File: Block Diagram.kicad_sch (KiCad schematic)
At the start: 0 parts

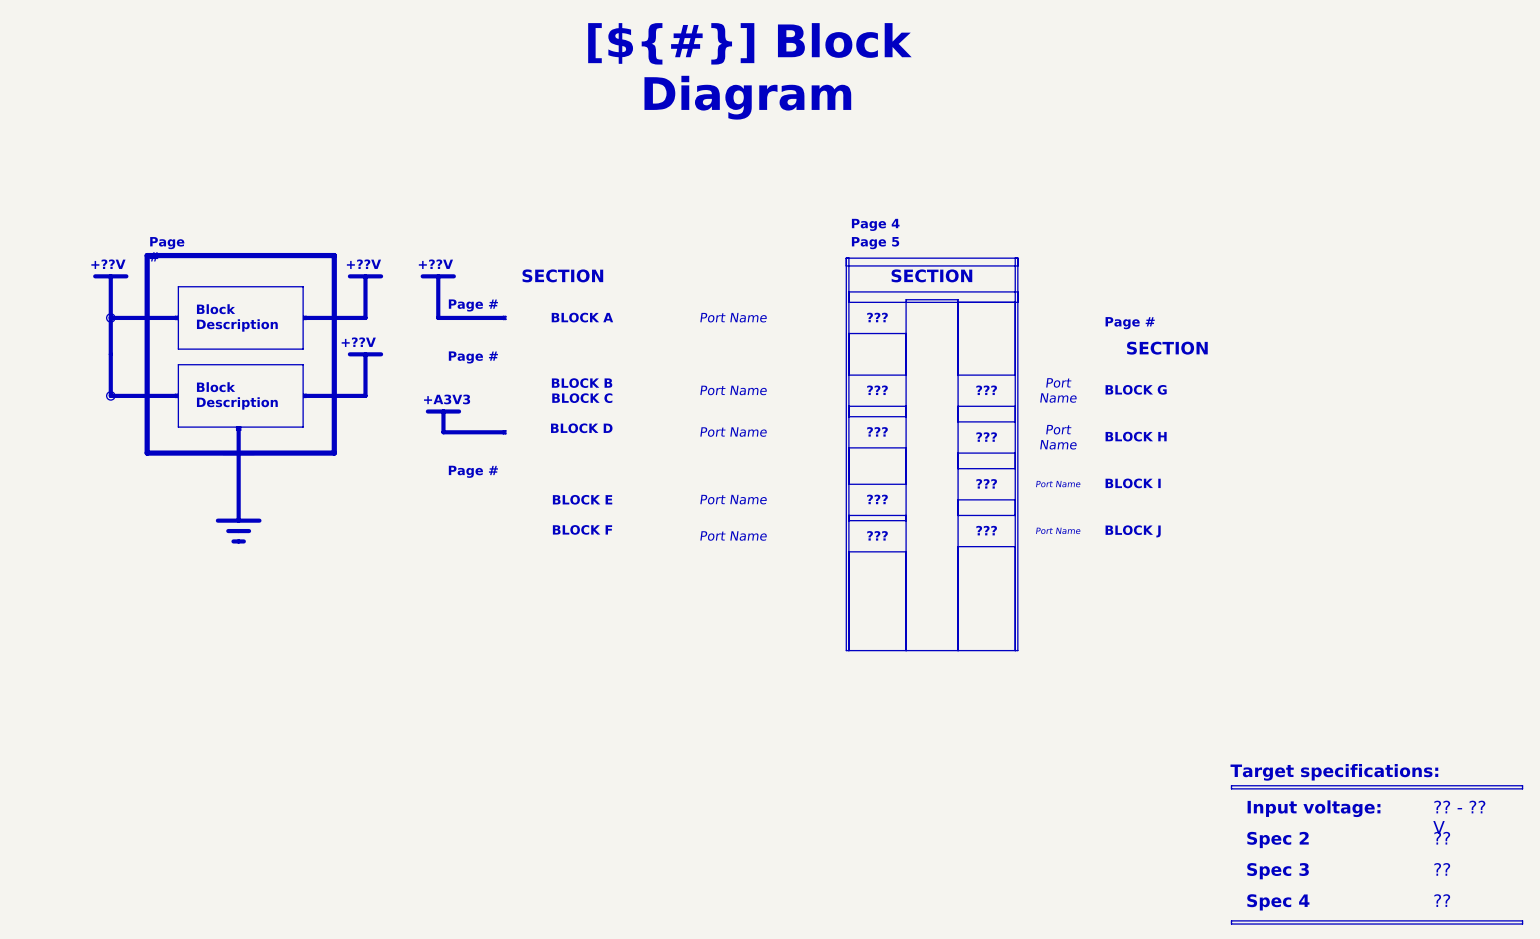
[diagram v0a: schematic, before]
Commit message: Fill template pages: block diagram, power sequencing, cover notes, architecture
- Block Diagram redrawn from the real design: phase path (MR60PW, shunts),
  current and voltage channels with their gains and bandwidths, AD7606C-18,
  power chain, target specifications
- Power - Sequencing: start-up curves taken from the LTspice simulations
  (boost soft-start, analog rails) and rail table with sources, levels
  and timings
- Cover page: real design notes instead of the template examples
- Project Architecture: power-supply block documented, contiguous page
  numbers (Power Supply is page 6)
- Revision History: one column fed by the [Unreleased] changelog section
- sheet titles shortened so they fit the cover-page index: INA241 - Phase
  Sensing, Power Supply - Analog Rails

Sheet-level polylines carry no fill attribute (KiBot schematic reader).

Co-Authored-By: Claude Opus 5.5 <noreply@anthropic.com>
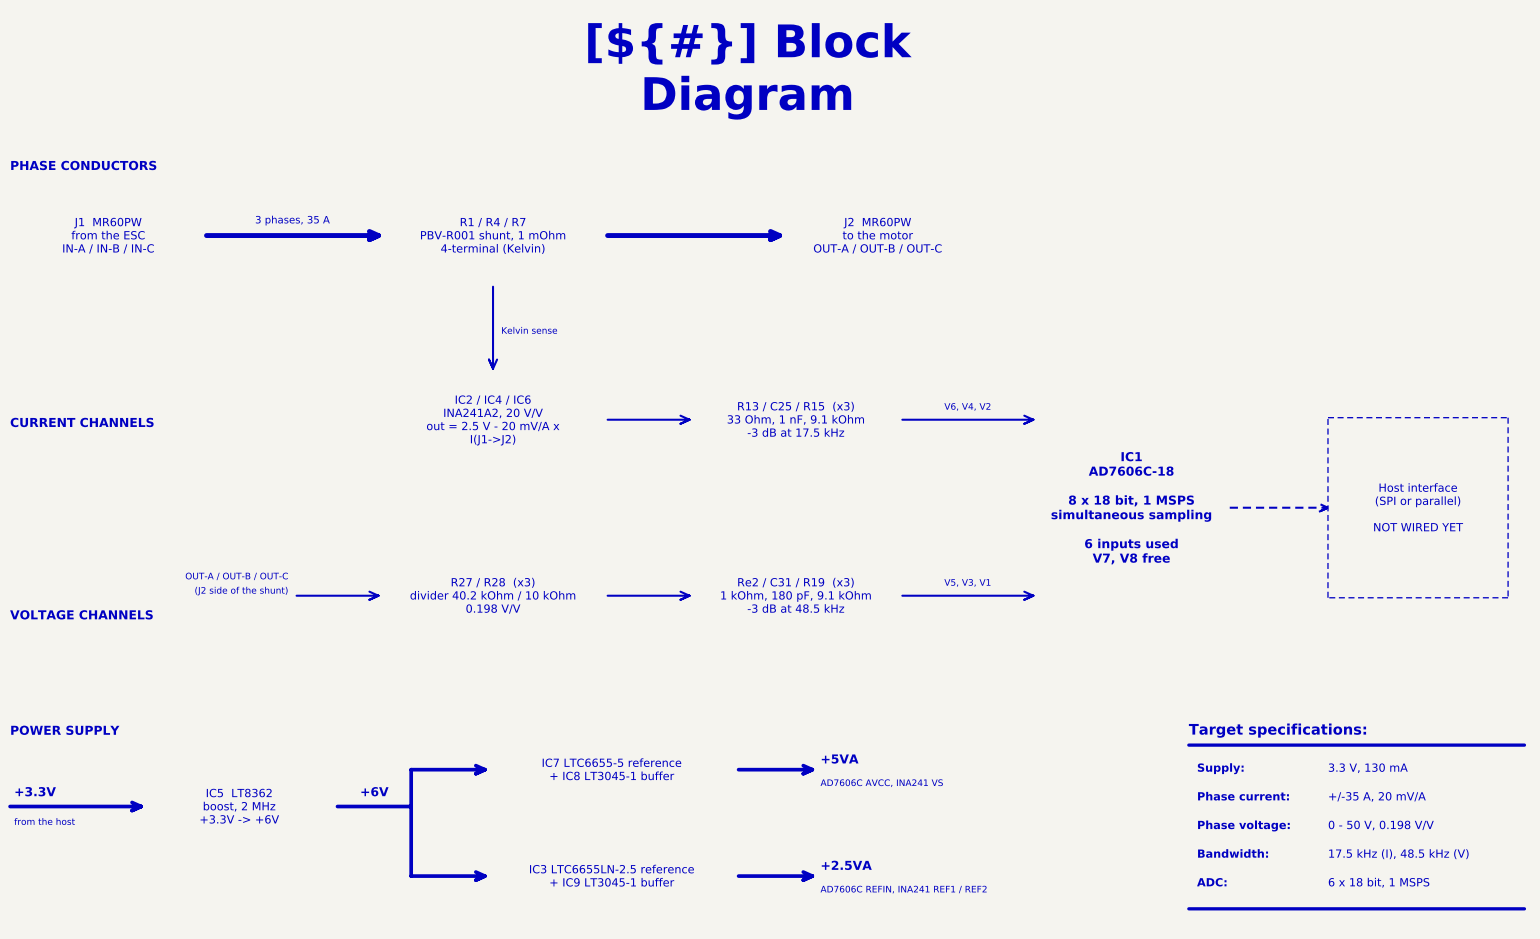
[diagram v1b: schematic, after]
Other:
- note added: "(J2 side of the shunt)"
- note added: "+/-35 A, 20 mV/A"
- note added: "+2.5VA"
- note added: "+3.3V"
- note added: "+5VA"
- note added: "+6V"
- note added: "0 - 50 V, 0.198 V/V"
- note added: "17.5 kHz (I), 48.5 kHz (V)"
- note added: "3 phases, 35 A"
- note added: "3.3 V, 130 mA"
- note added: "6 x 18 bit, 1 MSPS"
- note added: "AD7606C AVCC, INA241 VS"
- note added: "AD7606C REFIN, INA241 REF1 / REF2"
- note added: "ADC:"
- note added: "Bandwidth:"
- note added: "CURRENT CHANNELS"
- note added: "Kelvin sense"
- note added: "OUT-A / OUT-B / OUT-C"
- note added: "PHASE CONDUCTORS"
- note added: "POWER SUPPLY"
- note added: "Phase current:"
- note added: "Phase voltage:"
- note added: "Supply:"
- note added: "Target specifications:"
- note added: "V5, V3, V1"
- note added: "V6, V4, V2"
- note added: "VOLTAGE CHANNELS"
- note added: "from the host"
- note removed: "+??V"
- note removed: "+A3V3"

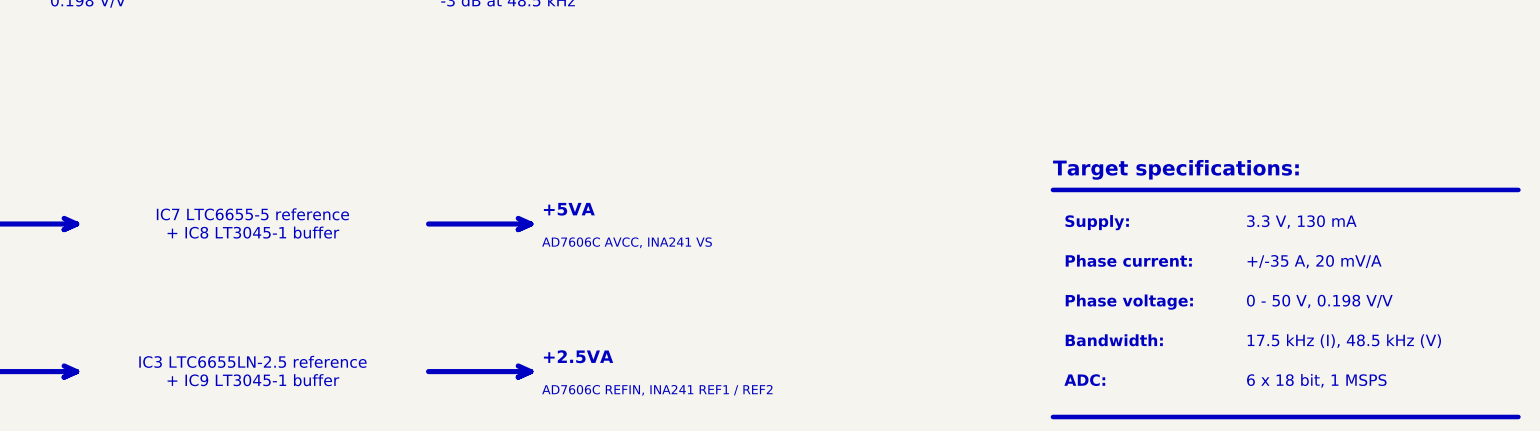
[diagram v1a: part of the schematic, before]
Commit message: Fix the +2.5VA reference, add XT60PW-M connectors, predict measurement quality
- IC3: LTC6655LN-2.5 replaced by the standard LTC6655-2.5, pin 6 is now
  VOUT_S tied to VOUT_F (the LN version has NR on that pin)
- R12: 49.9k -> 24.9k on the SET pin of IC9, +2.5VA = 2.500 V instead of
  2.549 V; both points removed from the README design review
- J5, J6: two Amass XT60PW-M added on the Connectors sheet and on the PCB,
  with symbol, footprint and 3D model in lib/. Their power pins are not
  wired yet
- Simulations 07 (ESC PWM waveforms through both channels) and 08 (Monte
  Carlo on the tolerances), analysed by measurement_quality.py into
  measurement_quality.md; plot style shared in plotstyle.py
- Simulations 01, 02, 04, results.md and their figures redone for the
  corrected rail
- README, README template and CHANGELOG updated; all sheets re-saved from
  KiCad

Co-Authored-By: Claude Opus 5.5 <noreply@anthropic.com>
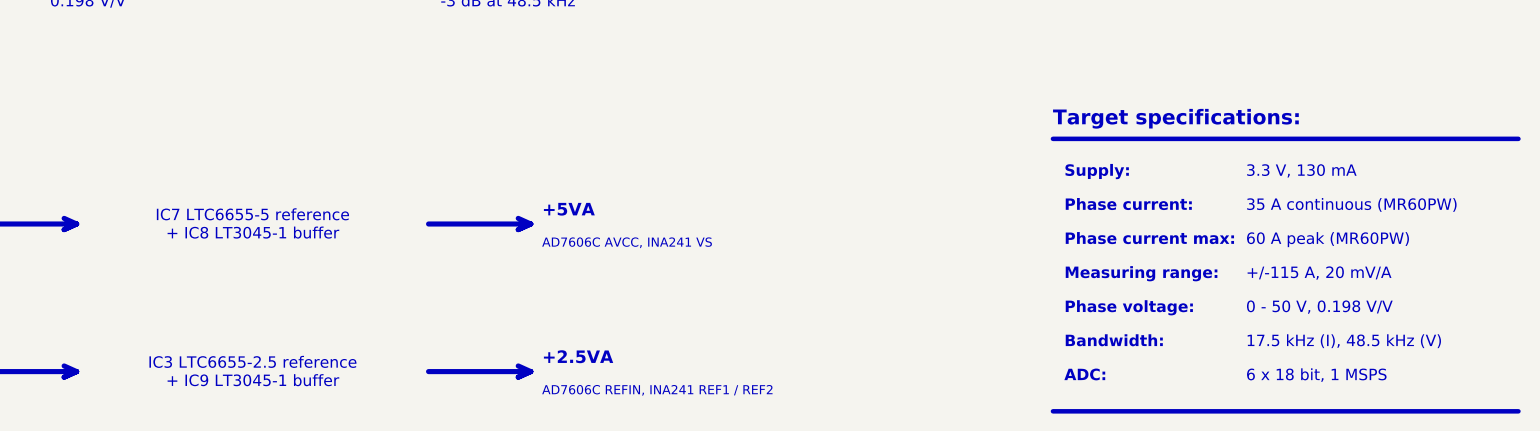
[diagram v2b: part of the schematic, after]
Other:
- note added: "+/-115 A, 20 mV/A"
- note added: "35 A continuous (MR60PW)"
- note added: "60 A peak (MR60PW)"
- note added: "Measuring range:"
- note added: "Phase current max:"
- note removed: "+/-35 A, 20 mV/A"

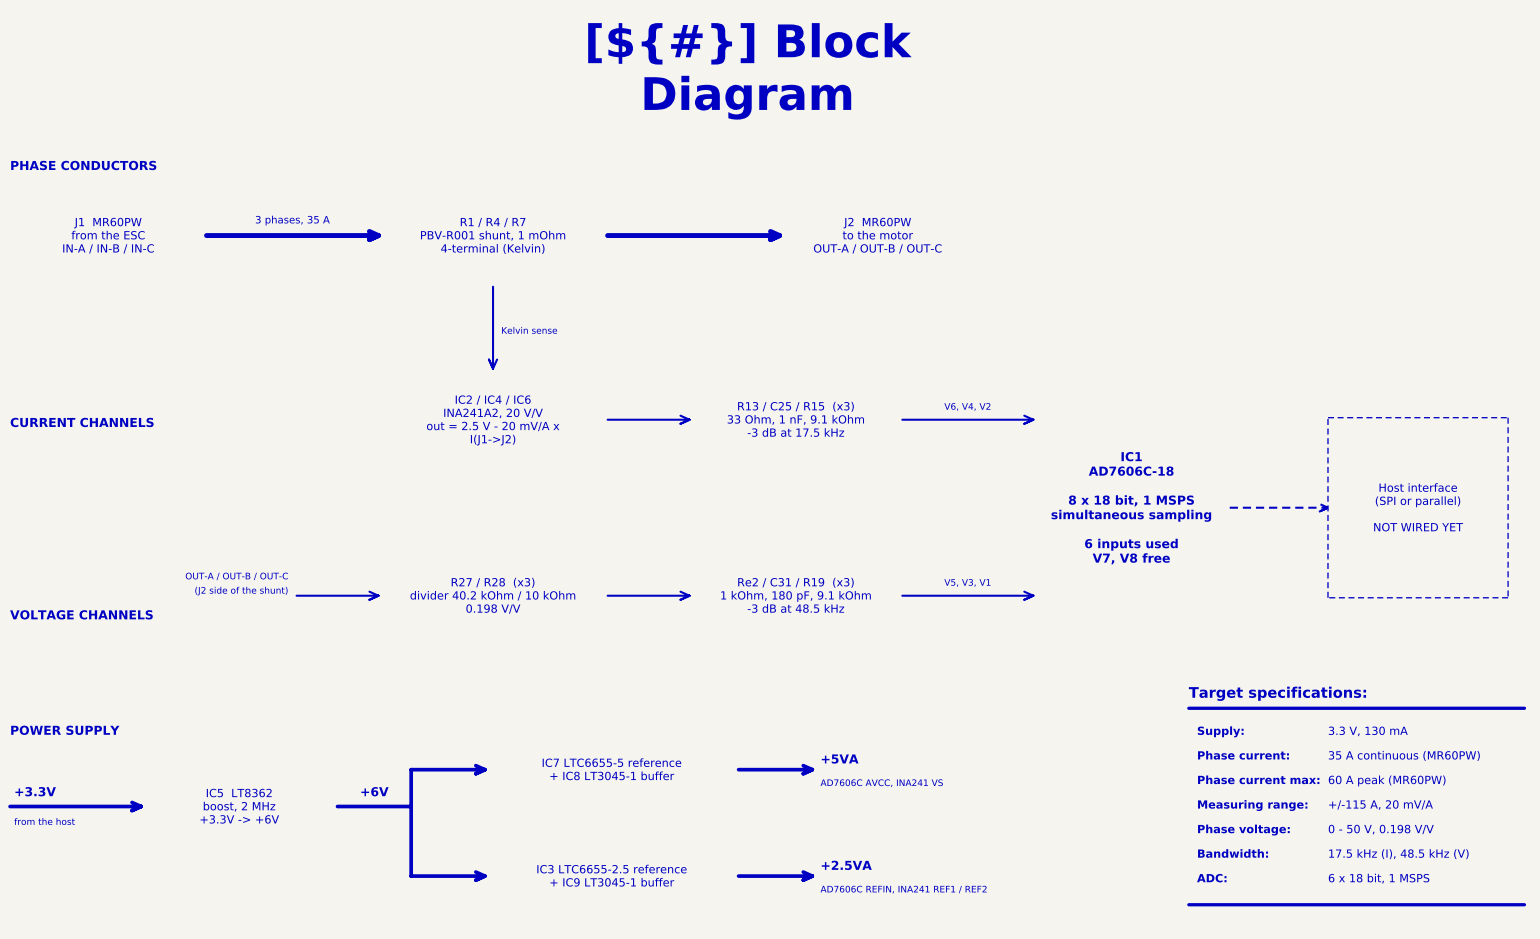
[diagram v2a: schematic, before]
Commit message: Smaller boost inductor, white board, openEMS and thermal simulations
- L1: Wurth 744373965022 (13.5 x 12.5 mm) -> WE-MAPI 4030 74438357022
  (2.2 uH, 4.1 x 4.1 x 3.1 mm, Isat 4.6 A at -10 %, above the 3.1 A LT8362
  switch limit). Footprint and STEP from the KiCad library, copied to lib/.
- Board: solder mask white (custom opaque #F4F4F0F5, the KiCad "White"
  preset renders pink over copper), silkscreen black. kibot_globals.yaml
  names the colours so the fabrication notes print WHITE / BLACK.
- Simulation/openEMS: inductance of the PBV shunts seen by the INA241
  inputs on the routed copper (results.md, figures in Images/Simulation).
- Simulation/Thermal: current density and temperature of the power paths.
- LTspice simulations, figures and README updated; sim07 DC bus figure.
- 3D animation (Images/OPEN_PHASE.mp4, OPEN_PHASE-spin.gif) on the white board.
- XT60PW-F footprint and model, bottom silkscreen cartouches.

Co-Authored-By: Claude Opus 5.5 <noreply@anthropic.com>
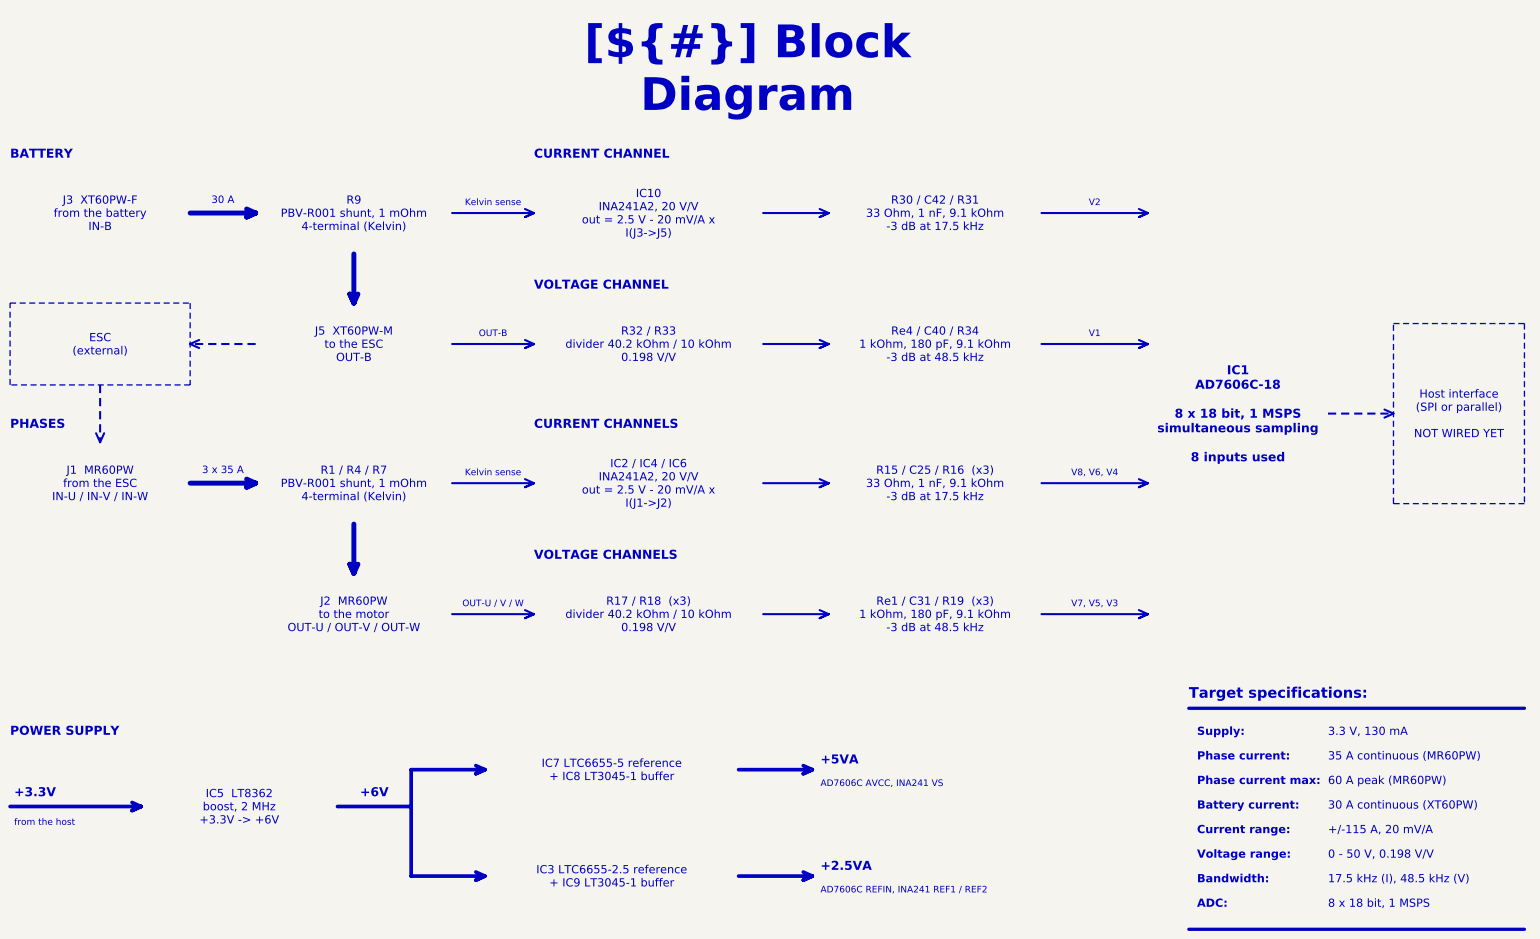
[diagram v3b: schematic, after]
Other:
- note added: "3 x 35 A"
- note added: "30 A"
- note added: "30 A continuous (XT60PW)"
- note added: "8 x 18 bit, 1 MSPS"
- note added: "BATTERY"
- note added: "Battery current:"
- note added: "CURRENT CHANNEL"
- note added: "Current range:"
- note added: "OUT-B"
- note added: "OUT-U / V / W"
- note added: "PHASES"
- note added: "V1"
- note added: "V2"
- note added: "V7, V5, V3"
- note added: "V8, V6, V4"
- note added: "VOLTAGE CHANNEL"
- note added: "Voltage range:"
- note removed: "(J2 side of the shunt)"
- note removed: "3 phases, 35 A"
- note removed: "6 x 18 bit, 1 MSPS"
- note removed: "Measuring range:"
- note removed: "OUT-A / OUT-B / OUT-C"
- note removed: "PHASE CONDUCTORS"
- note removed: "Phase voltage:"
- note removed: "V5, V3, V1"
- note removed: "V6, V4, V2"
